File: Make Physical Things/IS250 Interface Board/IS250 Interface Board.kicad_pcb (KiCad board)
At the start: 2 copper layers, 176.3 x 106.7 mm, 62 parts, among them J1 24_Pin_Reorg, J2 16_Pin, J3 Barrel_Jack, J4 XT60-M, J5 Conn_01x02, J6 Conn_01x02, J7 Conn_01x02, J8 Conn_01x02, Q1 PN2222A, Q10 PN2222A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

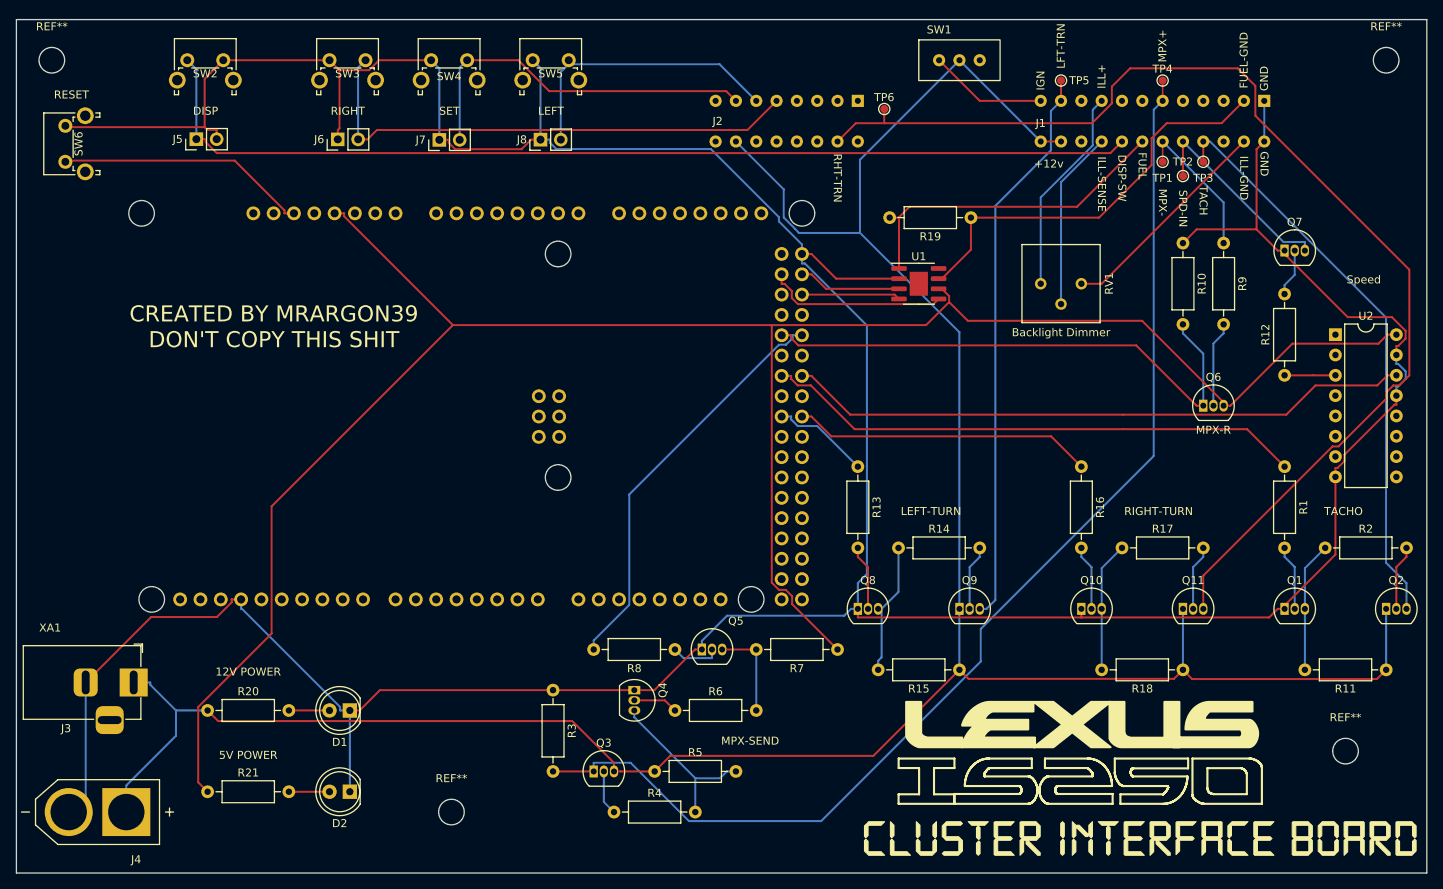
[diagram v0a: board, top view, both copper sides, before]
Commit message: Fixed Error
Updated footprints for custom objects with correct hole sizing, and fixed routing errors caused by the change.
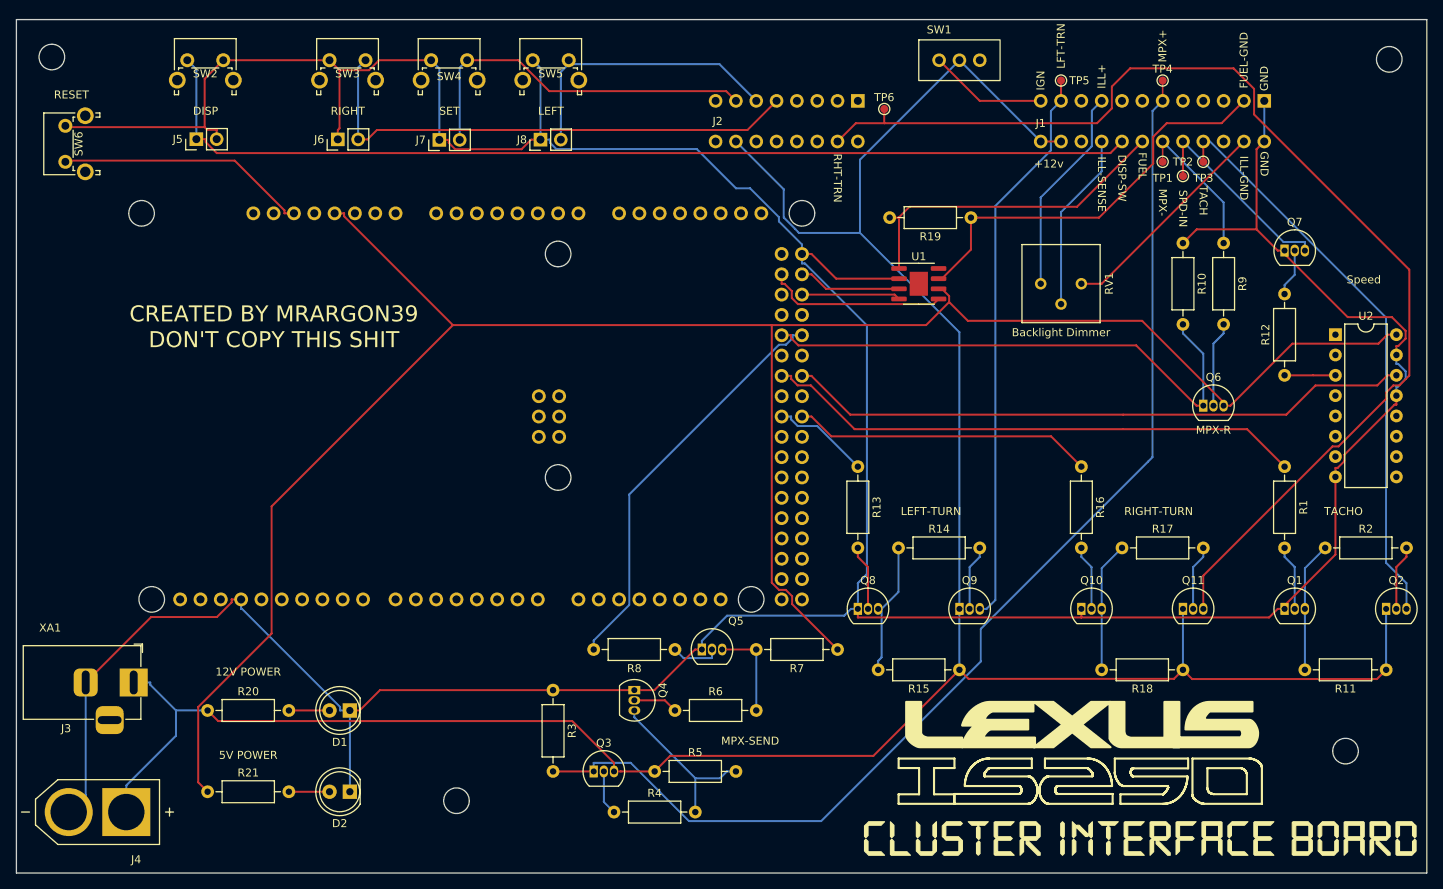
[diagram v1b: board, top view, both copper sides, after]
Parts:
- moved REF** 1.55 mm to (120.0, 138.3)
- moved REF** 0.41 mm to (236.6, 45.6)
- moved REF** 0.40 mm to (69.4, 45.3)

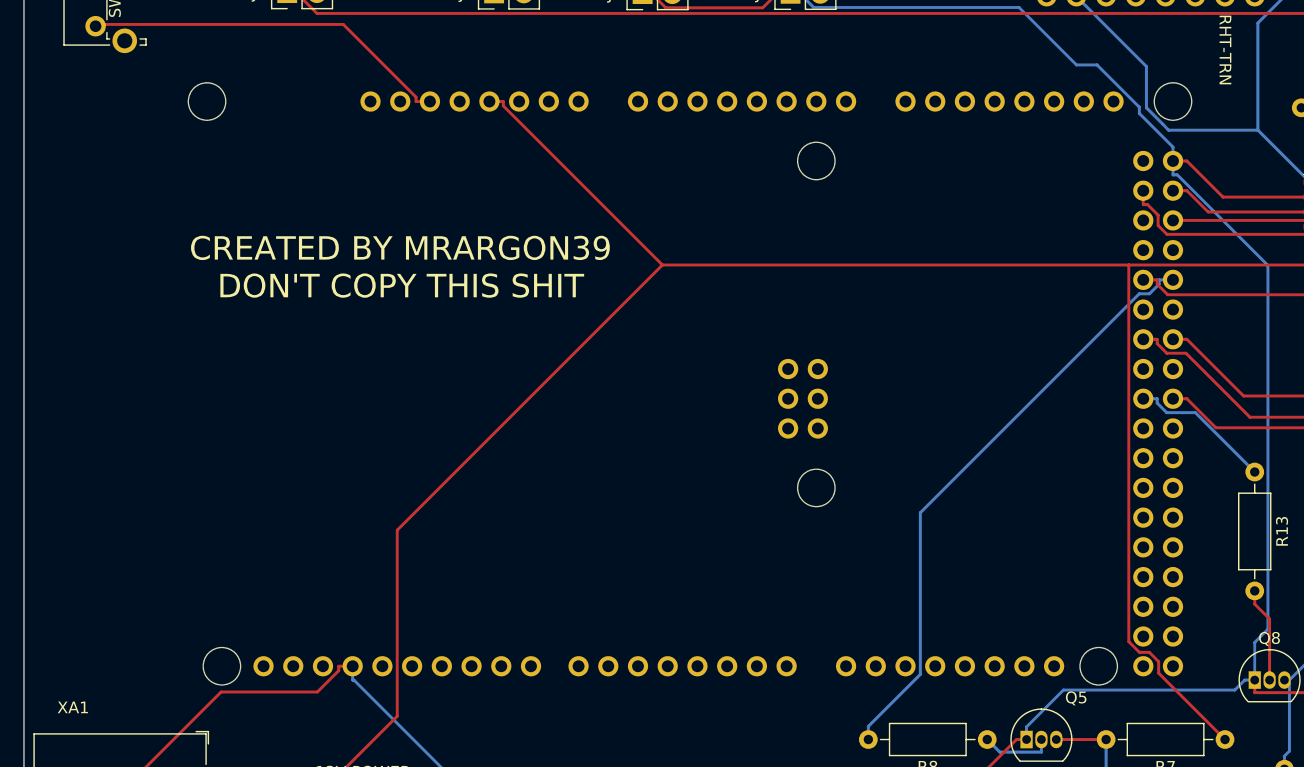
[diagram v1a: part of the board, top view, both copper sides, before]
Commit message: Updated Silkscreen
Fixed the silkscreen for the arduino socket
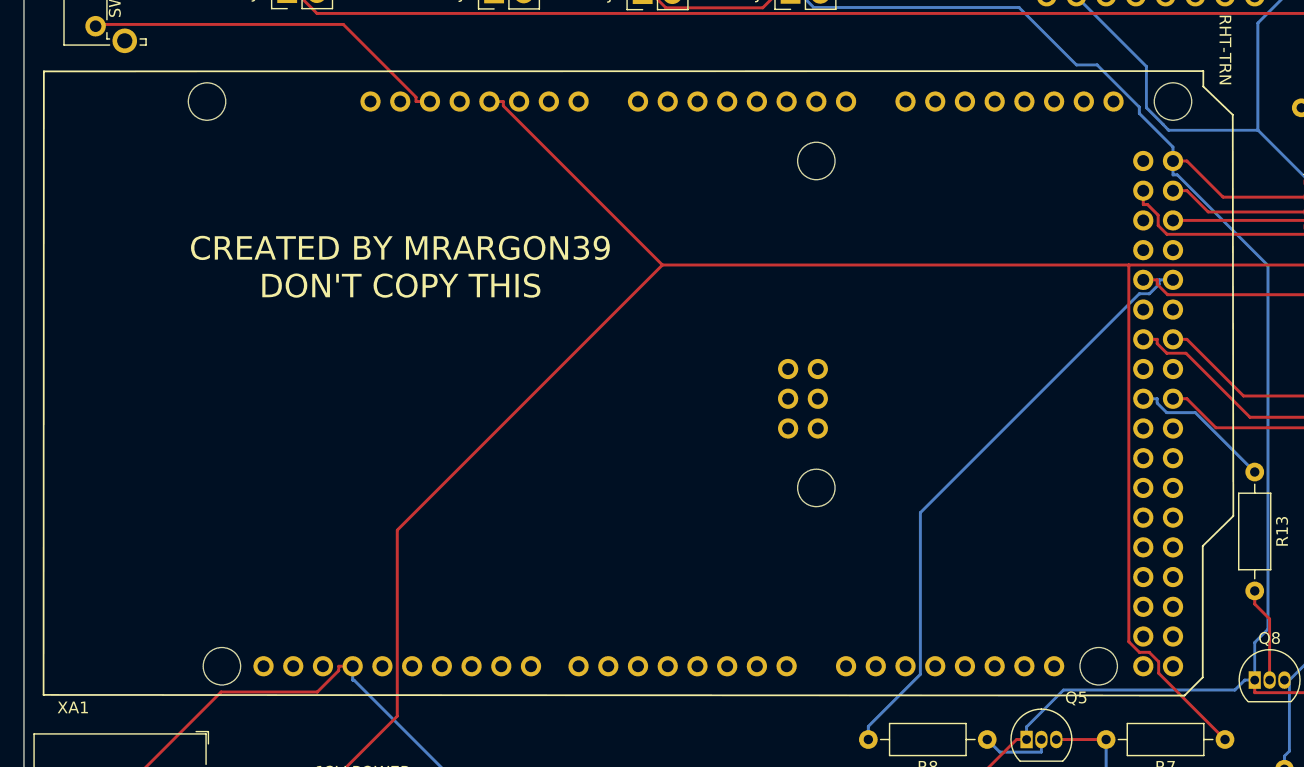
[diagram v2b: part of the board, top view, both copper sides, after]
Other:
- board text added: "CREATED BY MRARGON39 DON'T COPY THIS"
- board text removed: "CREATED BY MRARGON39 DON'T COPY THIS SHIT"
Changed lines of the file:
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@@
+  (gr_poly
+    (pts
+      (xy 165.7858 63.5762)
+      (xy 168.3004 65.9892)
+      (xy 168.3512 100.2792)
+      (xy 165.735 102.8446)
+      (xy 165.735 114.0714)
+      (xy 164.1856 115.6208)
+      (xy 66.675 115.57)
+      (xy 66.7004 62.2808)
+      (xy 165.7858 62.2554)
+    ) (layer "F.SilkS") (width 0.15) (fill none))
   (gr_poly
     (pts
@@
     (effects (font (size 1 1) (thickness 0.15)))
   )
-  (gr_text "CREATED BY MRARGON39\nDON'T COPY THIS SHIT" (at 97.19 79.05) (layer "F.SilkS")
+  (gr_text "CREATED BY MRARGON39\nDON'T COPY THIS" (at 97.19 79.05) (layer "F.SilkS")
     (effects (font (size 2 2) (thickness 0.15)))
   )

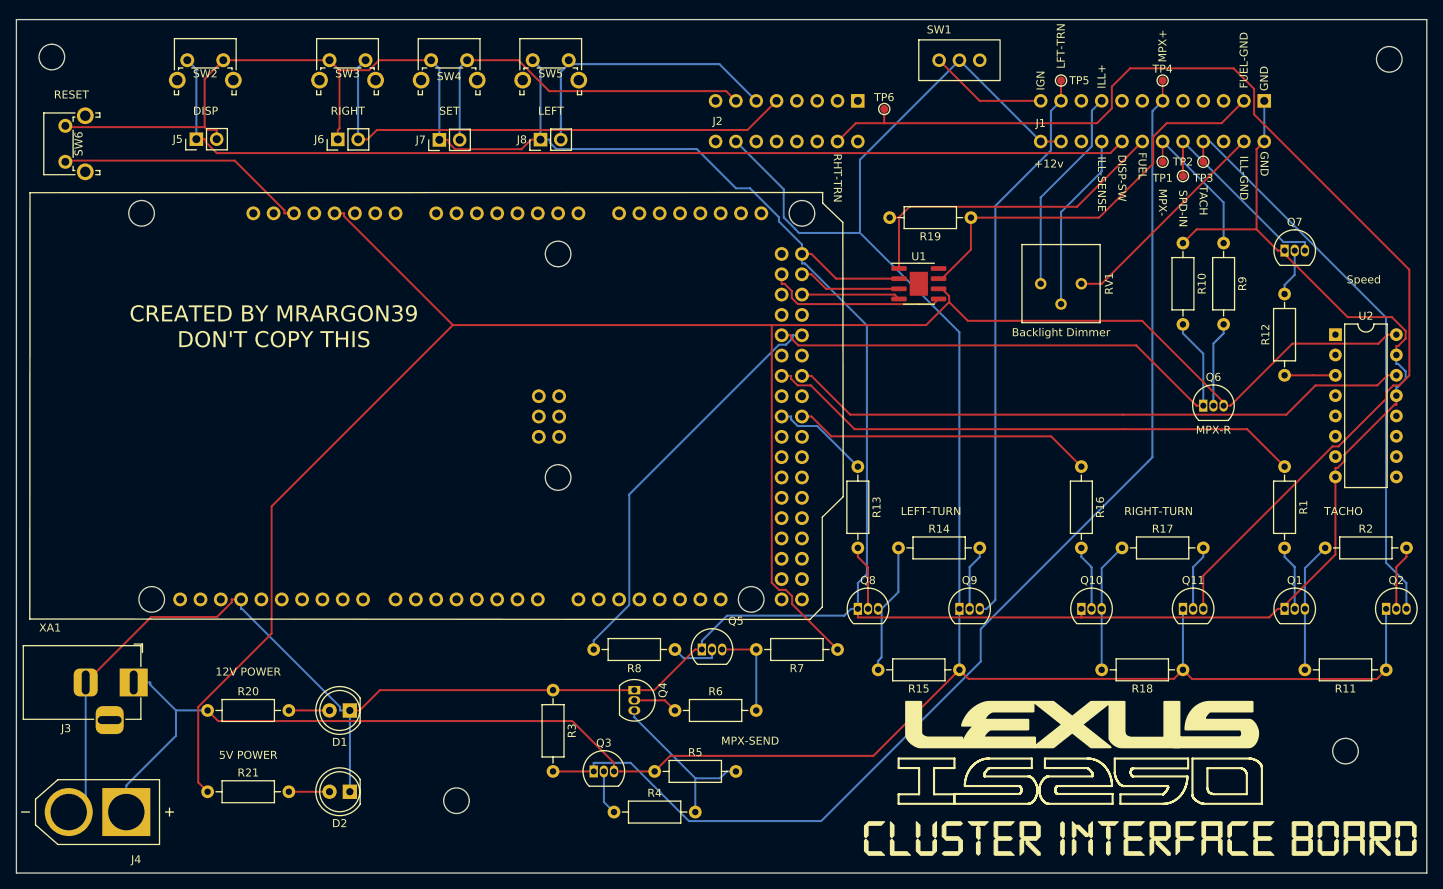
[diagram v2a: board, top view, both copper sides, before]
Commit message: Updated Silkscreen
Added resistor values to the silkscreen
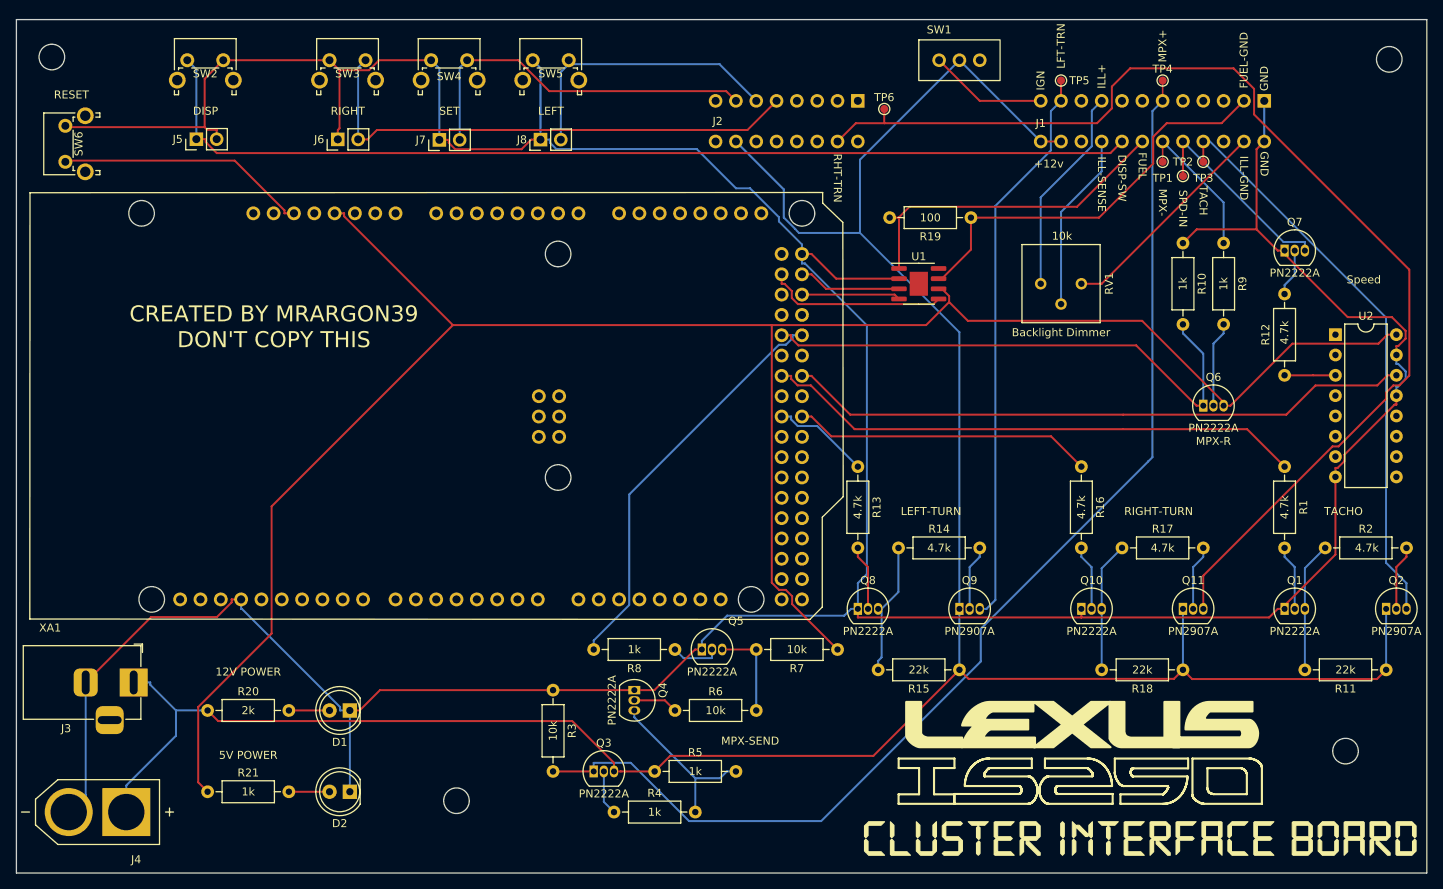
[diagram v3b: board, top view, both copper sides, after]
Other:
- board text added: "10k"
